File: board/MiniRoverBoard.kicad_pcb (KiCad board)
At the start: 2 copper layers, 103.4 x 63.8 mm, 50 parts, among them J1 DEBUG, Q1 NMOS, Q2 BSS138, U2 OKI, U3 Opamp_Dual, U4 LT1910, U7 ESP32-S2-DEVKITM-1U, U8 Opamp_Dual

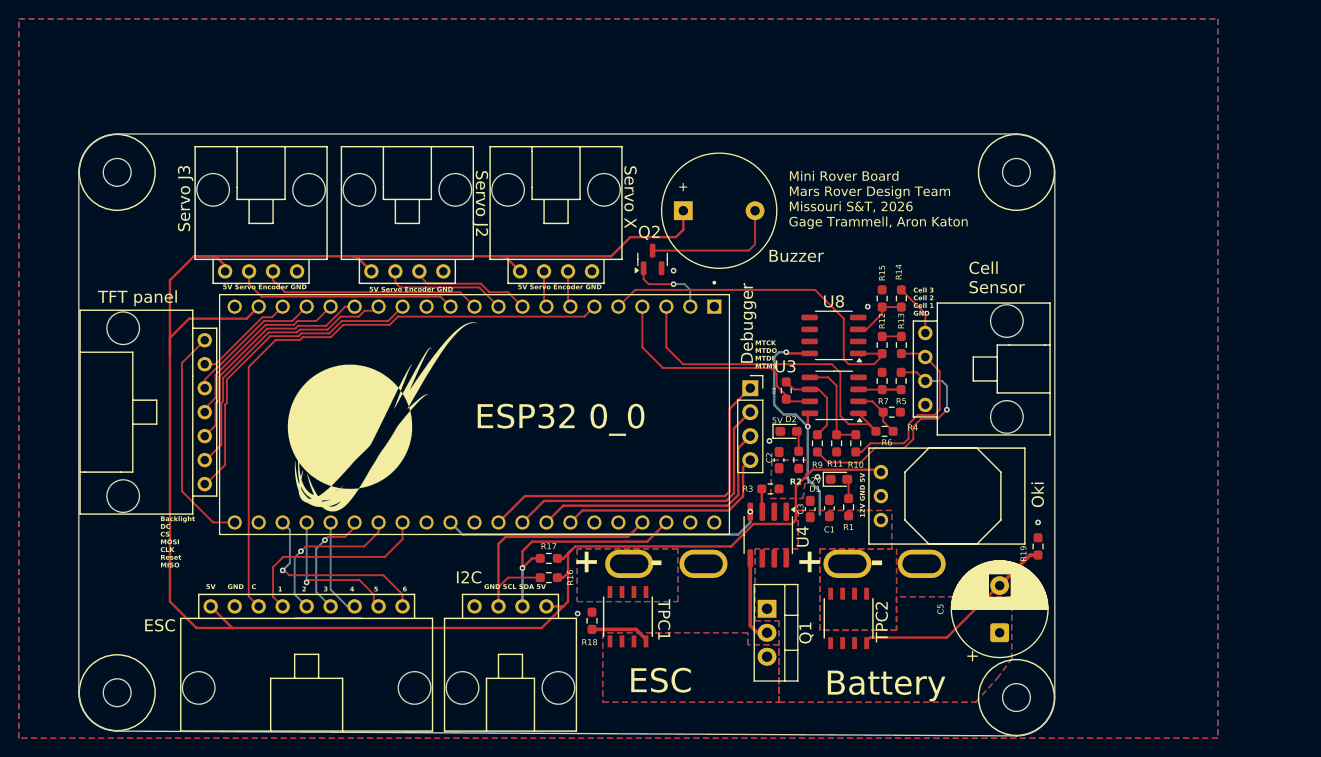
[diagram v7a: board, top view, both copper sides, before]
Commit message: Updated Dimensions
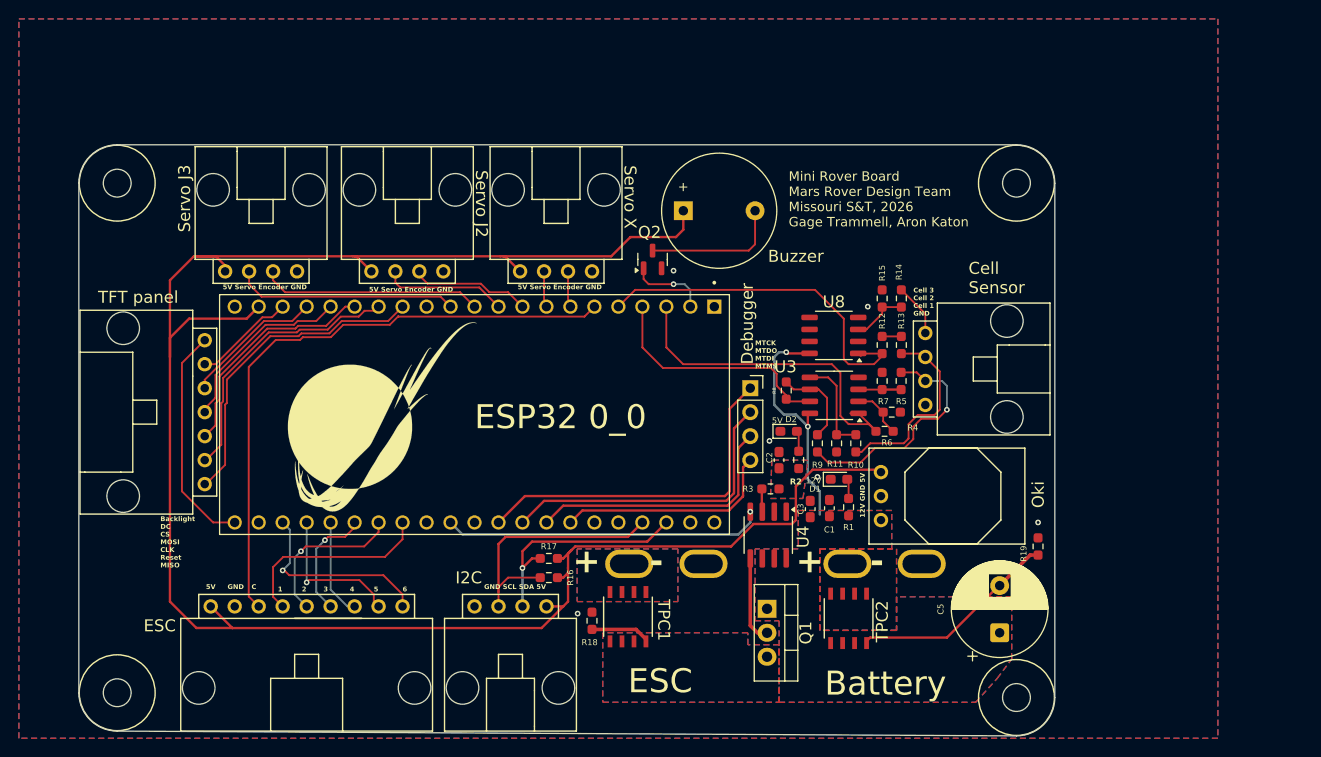
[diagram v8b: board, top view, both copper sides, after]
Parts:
- moved H3 1.14 mm to (143.8, 42.8)
- moved H4 1.14 mm to (48.5, 42.8)
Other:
- board size 103.4 x 63.8 mm -> 103.4 x 62.6 mm
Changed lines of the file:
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@@
 	(footprint "MRDT_Drill_Holes:4_40_Hole"
 		(layer "F.Cu")
-		(at 143.764 41.656)
+		(at 143.764 42.799)
 		(property "Reference" "H3"
 			(at -0.00508 0.50508 0)
@@
 	(footprint "MRDT_Drill_Holes:4_40_Hole"
 		(layer "F.Cu")
-		(at 48.514 41.656)
+		(at 48.514 42.799)
 		(property "Reference" "H4"
 			(at -0.00508 0.50508 0)
@@
 	)
 	(gr_arc
-		(start 44.45 41.656)
-		(mid 45.640318 38.782318)
-		(end 48.514 37.592)
+		(start 44.45 42.799)
+		(mid 45.640318 39.925318)
+		(end 48.514 38.735)
 		(stroke
 			(width 0.05)
@@
 	(gr_line
 		(start 147.828 97.282)
-		(end 147.828 41.656)
+		(end 147.828 42.799)
 		(stroke
 			(width 0.05)
@@
 	)
 	(gr_line
-		(start 44.45 41.656)
+		(start 44.45 42.799)
 		(end 44.45 96.774)
 		(stroke
@@
 	)
 	(gr_line
-		(start 143.764 37.592)
-		(end 48.514 37.592)
+		(start 143.764 38.735)
+		(end 48.514 38.735)
 		(stroke
 			(width 0.05)
@@
 	)
 	(gr_arc
-		(start 143.764 37.592)
-		(mid 146.637682 38.782318)
-		(end 147.828 41.656)
+		(start 143.764 38.735)
+		(mid 146.637682 39.925318)
+		(end 147.828 42.799)
 		(stroke
 			(width 0.05)
